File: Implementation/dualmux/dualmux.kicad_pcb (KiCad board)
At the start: 2 copper layers, 127 x 63.5 mm, 27 parts, among them U1 74HC00, U10 74HC00, U11 74HC00, U12 74HC00, U13 74HC00, U2 74HC00, U3 74HC00, U4 74HC00, U5 74HC00, U6 74HC00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

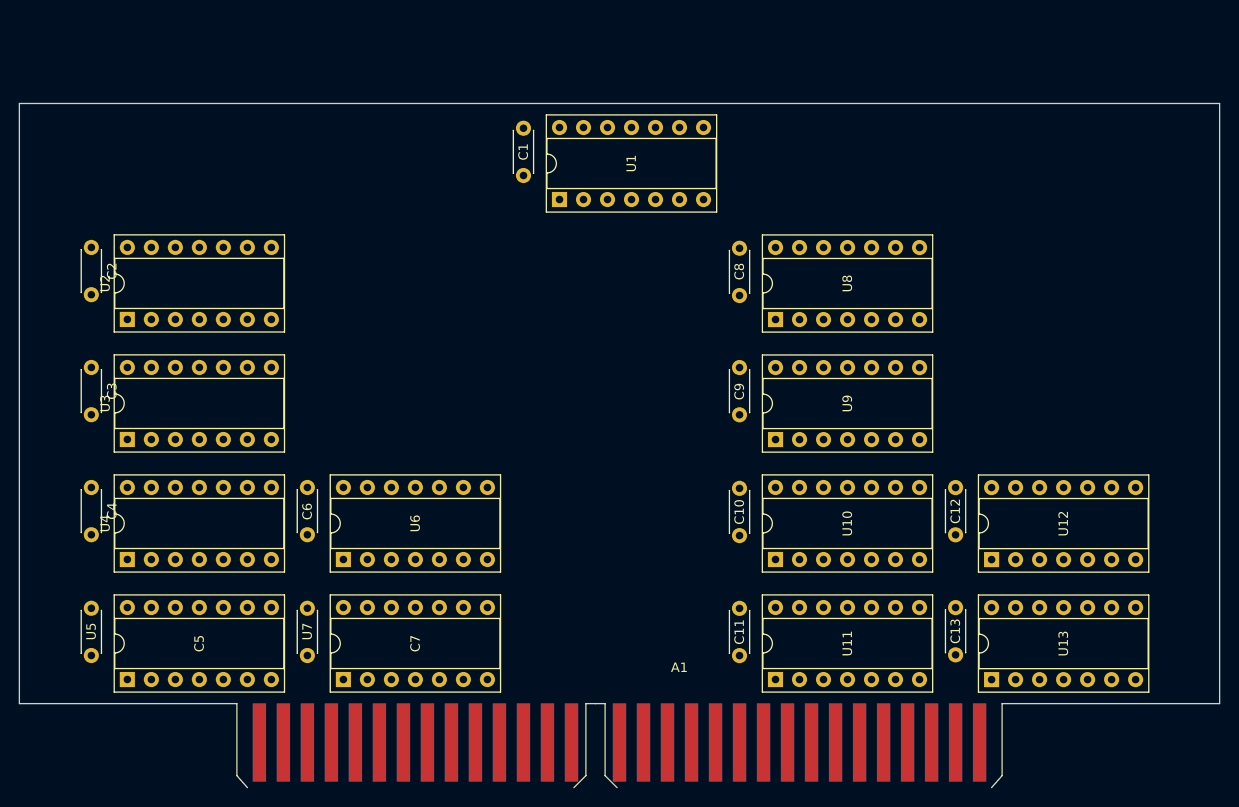
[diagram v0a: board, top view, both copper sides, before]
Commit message: Some of the routing done, need to figure out how to get everything to the connector
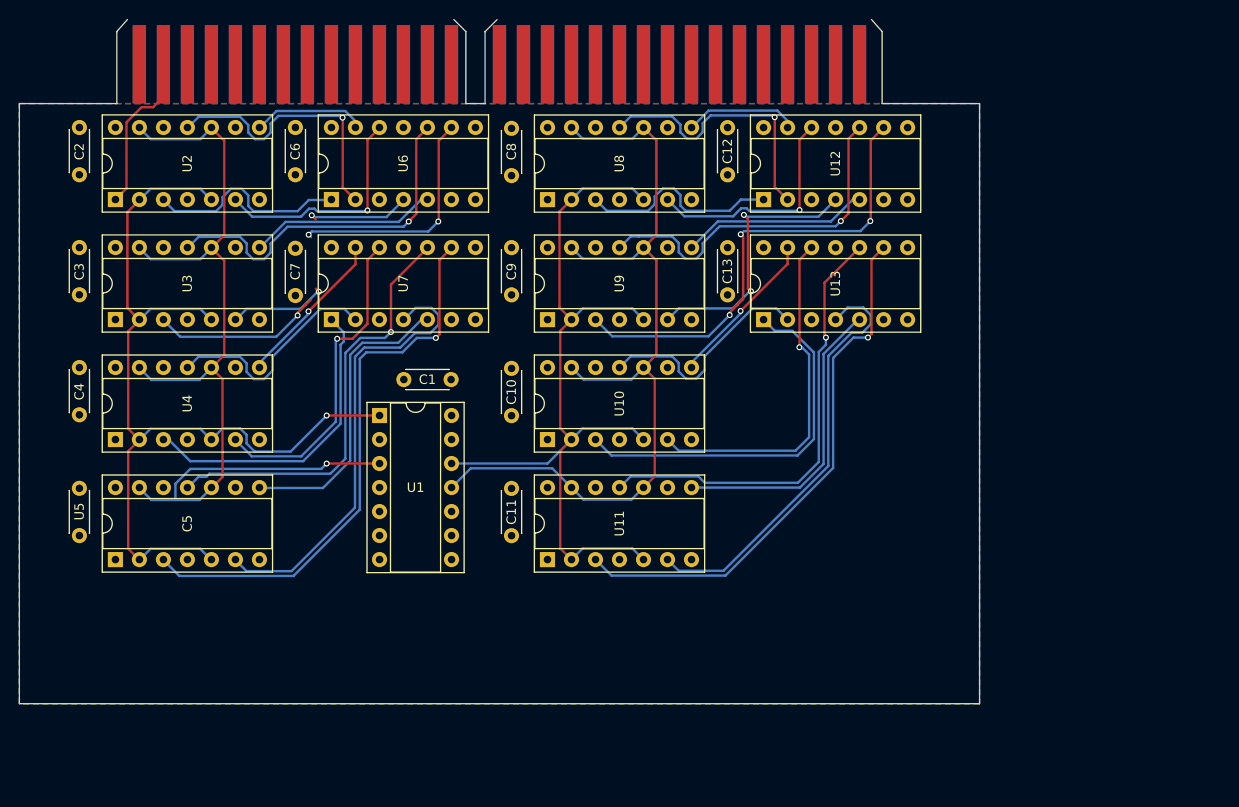
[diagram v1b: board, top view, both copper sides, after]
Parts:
- A1: moved to B.Cu
- moved A1 64.7 mm to (203.2, 63.5)
- moved C12 45.1 mm to (227.3, 71.0)
- moved C13 45.1 mm to (227.3, 83.8)
- moved U12 45.1 mm to (231.1, 73.7)
- moved U13 45.1 mm to (231.1, 86.4)
- moved C7 38.1 mm to (181.6, 78.8)
- moved U6 38.1 mm to (185.4, 73.7)
- moved U7 38.1 mm to (185.4, 86.4)
- moved C6 38.1 mm to (181.6, 71.0)
- moved U1 29.7 mm to (190.5, 96.5), turned to 0 degrees
- moved C1 27.7 mm to (198.1, 92.7), turned to 180 degrees
- moved C10 27.3 mm to (204.5, 91.5)
- moved C11 27.3 mm to (204.5, 104.2)
- moved C8 27.3 mm to (204.5, 66.1)
- moved C9 27.3 mm to (204.5, 78.8)
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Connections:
- net /MuxModule1/B_SEL renamed //A_SEL
- net /MuxModule2/B_SEL renamed //B_SEL
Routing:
- net //A_SEL: track 0.00 -> 100.1 mm, vias 0 -> 1
- net /A_SEL: track 0.00 -> 96.9 mm, vias 0 -> 1
- net //B_SEL: track 0.00 -> 90.2 mm
- net /B_SEL: track 0.00 -> 89.2 mm
- net Net-(U5-Pad3): track 0.00 -> 59.5 mm, vias 0 -> 1
- net Net-(U11-Pad3): track 0.00 -> 57.0 mm, vias 0 -> 1
- net Net-(U12-Pad9): track 0.00 -> 49.9 mm, vias 0 -> 3
- net Net-(U5-Pad6): track 0.00 -> 47.7 mm
- net Net-(U11-Pad11): track 0.00 -> 47.4 mm, vias 0 -> 1
- net Net-(U5-Pad11): track 0.00 -> 45.4 mm, vias 0 -> 1
- net Net-(U11-Pad6): track 0.00 -> 45.2 mm
- net Net-(U3-Pad3): track 0.00 -> 43.3 mm, vias 0 -> 3
- net Net-(U10-Pad3): track 0.00 -> 40.5 mm
- net Net-(U3-Pad11): track 0.00 -> 38.4 mm, vias 0 -> 1
- net Net-(U12-Pad10): track 0.00 -> 38.4 mm, vias 0 -> 1
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- added copper zone on F.Cu, net +5V
- added copper zone on B.Cu, net GND
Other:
- board size 127 x 63.5 mm -> 101.6 x 63.5 mm
- rule pad_to_mask_clearance: 0 -> 0.038

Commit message: Most of mux routing
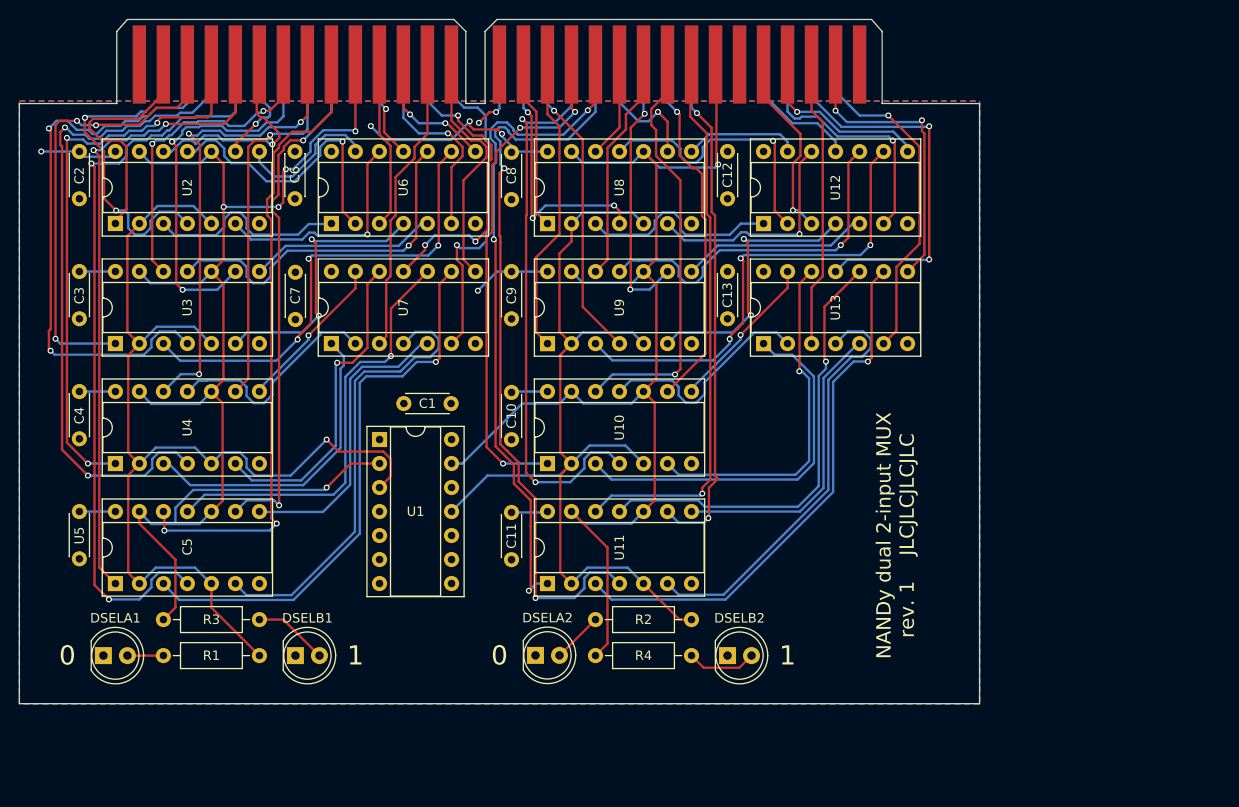
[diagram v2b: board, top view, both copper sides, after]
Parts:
- added DSELA1: RED, LED_THT:LED_D5.0mm, F.Cu at (161.3, 121.9)
- added DSELA2: RED, LED_THT:LED_D5.0mm, F.Cu at (207.0, 121.9)
- added DSELB1: GREEN, LED_THT:LED_D5.0mm, F.Cu at (181.6, 121.9)
- added DSELB2: GREEN, LED_THT:LED_D5.0mm, F.Cu at (227.3, 121.9)
- added R1: 1k, Resistor_THT:R_Axial_DIN0207_L6.3mm_D2.5mm_P10.16mm_Horizontal, F.Cu at (177.8, 121.9)
- added R2: 1k, Resistor_THT:R_Axial_DIN0207_L6.3mm_D2.5mm_P10.16mm_Horizontal, F.Cu at (223.5, 118.1)
- added R3: 1k, Resistor_THT:R_Axial_DIN0207_L6.3mm_D2.5mm_P10.16mm_Horizontal, F.Cu at (167.6, 118.1)
- added R4: 1k, Resistor_THT:R_Axial_DIN0207_L6.3mm_D2.5mm_P10.16mm_Horizontal, F.Cu at (213.4, 121.9)
- moved C1 2.54 mm to (198.1, 95.2)
- moved C3 2.54 mm to (158.8, 81.3)
- moved C4 2.54 mm to (158.8, 94.0)
- moved C7 2.54 mm to (181.6, 81.4)
- moved C8 2.54 mm to (204.5, 68.7)
- moved C9 2.54 mm to (204.5, 81.3)
- moved U1 2.54 mm to (190.5, 99.1)
- moved U2 2.54 mm to (162.6, 76.2)
- moved U3 2.54 mm to (162.6, 88.9)
- moved U6 2.54 mm to (185.4, 76.2)
- moved U7 2.54 mm to (185.4, 88.9)
- moved C10 2.54 mm to (204.5, 94.1)
- moved C11 2.54 mm to (204.5, 106.8)
- moved C2 2.54 mm to (158.8, 68.6)
- moved U10 2.54 mm to (208.3, 101.6)
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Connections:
- U1 pad 1: /A_SEL -> +5V
- U1 pad 11: //B_SEL -> /nB_SEL
- U1 pad 12: /B_SEL -> +5V
- U1 pad 13: +5V -> /B_SEL
- U1 pad 2: +5V -> /A_SEL
- U1 pad 3: //A_SEL -> /nA_SEL
- U10 pad 10: //B_SEL -> /B_SEL
- U10 pad 13: //B_SEL -> /B_SEL
- U10 pad 2: /B_SEL -> /nB_SEL
- U10 pad 5: /B_SEL -> /nB_SEL
- U11 pad 10: //B_SEL -> /B_SEL
- U11 pad 13: //B_SEL -> /B_SEL
- U11 pad 2: /B_SEL -> /nB_SEL
- U11 pad 5: /B_SEL -> /nB_SEL
- U2 pad 10: //A_SEL -> /A_SEL
- U2 pad 13: //A_SEL -> /A_SEL
- U2 pad 2: /A_SEL -> /nA_SEL
- U2 pad 5: /A_SEL -> /nA_SEL
- U3 pad 10: //A_SEL -> /A_SEL
- U3 pad 13: //A_SEL -> /A_SEL
- U3 pad 2: /A_SEL -> /nA_SEL
- U3 pad 5: /A_SEL -> /nA_SEL
- U4 pad 10: //A_SEL -> /A_SEL
- U4 pad 13: //A_SEL -> /A_SEL
- U4 pad 2: /A_SEL -> /nA_SEL
- U4 pad 5: /A_SEL -> /nA_SEL
- U5 pad 10: //A_SEL -> /A_SEL
- U5 pad 13: //A_SEL -> /A_SEL
- U5 pad 2: /A_SEL -> /nA_SEL
- U5 pad 5: /A_SEL -> /nA_SEL
- U8 pad 10: //B_SEL -> /B_SEL
- U8 pad 13: //B_SEL -> /B_SEL
- U8 pad 2: /B_SEL -> /nB_SEL
- U8 pad 5: /B_SEL -> /nB_SEL
- U9 pad 10: //B_SEL -> /B_SEL
- U9 pad 13: //B_SEL -> /B_SEL
- U9 pad 2: /B_SEL -> /nB_SEL
- U9 pad 5: /B_SEL -> /nB_SEL
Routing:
- net /nA_SEL: track 0.00 -> 115.0 mm, vias 0 -> 1
- net //A_SEL: track 100.1 -> 0.00 mm, vias 1 -> 0
- net /nB_SEL: track 0.00 -> 98.0 mm
- net //B_SEL: track 90.2 -> 0.00 mm
- net /AA7: track 0.00 -> 80.4 mm, vias 0 -> 2
- net /AB7: track 0.00 -> 80.3 mm, vias 0 -> 2
- net /AA5: track 0.00 -> 71.8 mm, vias 0 -> 2
- net /AB6: track 0.00 -> 70.6 mm, vias 0 -> 3
- net /AA6: track 0.00 -> 68.6 mm, vias 0 -> 2
- net /BA6: track 0.00 -> 67.3 mm, vias 0 -> 2
- net /AA3: track 0.00 -> 61.4 mm, vias 0 -> 2
- net /AB5: track 0.00 -> 60.8 mm, vias 0 -> 2
- net /AA4: track 0.00 -> 60.5 mm, vias 0 -> 3
- net +5V: track 0.00 -> 60.2 mm, vias 0 -> 5
- net /BB6: track 0.00 -> 58.8 mm, vias 0 -> 1
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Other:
- board text added: "0"
- board text added: "1"
- board text added: "NANDy dual 2-input MUX rev. 1 JLCJLCJLCJLC"
